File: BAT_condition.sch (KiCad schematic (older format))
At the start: 2 parts

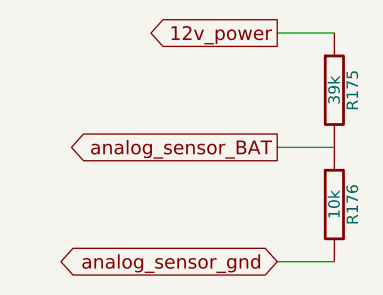
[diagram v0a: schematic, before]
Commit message: Removed LM1815 options. Now adaptive mode and square waves are the default,
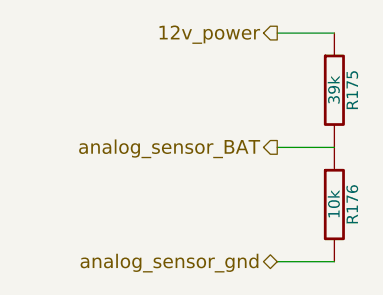
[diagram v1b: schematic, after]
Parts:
- R175: Field1 (none) -> newark,38K0371; Field2 (none) -> vendor1, smd w hem; Field3 (none) -> vendor2, thru w hem; Field4 (none) -> vendor2, smd w hem; Field5 (none) -> 250,mW; Field6 (none) -> 5,%; Field7 (none) -> carbon film; Field8 (none) -> other,more,stuff
- R176: Field1 (none) -> newark,38k0328; Field2 (none) -> vendor1, smd w hem; Field3 (none) -> vendor2, thru w hem; Field4 (none) -> vendor2, smd w hem; Field5 (none) -> 250,mW; Field6 (none) -> 5,%; Field7 (none) -> carbon film; Field8 (none) -> other,more,stuff
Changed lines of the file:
@@
-EESchema Schematic File Version 1
-LIBS:power,./freeEMS_lib,device,conn,linear,regul,74xx,cmos4000,adc-dac,memory,xilinx,special,microcontrollers,dsp,microchip,analog_switches,motorola,texas,intel,audio,interface,digital-audio,philips,display,cypress,siliconi,contrib,valves,./freeEMS_1.cache
+EESchema Schematic File Version 2  date Fri 02 Jul 2010 02:24:35 PM ART
+LIBS:power
+LIBS:freeEMS_lib
+LIBS:device
+LIBS:conn
+LIBS:linear
+LIBS:regul
+LIBS:74xx
+LIBS:cmos4000
+LIBS:adc-dac
+LIBS:memory
+LIBS:xilinx
+LIBS:special
+LIBS:microcontrollers
+LIBS:dsp
+LIBS:microchip
+LIBS:analog_switches
+LIBS:motorola
+LIBS:texas
+LIBS:intel
+LIBS:audio
+LIBS:interface
+LIBS:digital-audio
+LIBS:philips
+LIBS:display
+LIBS:cypress
+LIBS:siliconi
+LIBS:contrib
+LIBS:valves
+LIBS:freeEMS_1-cache
 EELAYER 23  0
 EELAYER END
@@
 Sheet 37 41
 Title "freeEMS 1.0"
-Date "15 nov 2008"
+Date "2 jul 2010"
 Rev "A.20"
 Comp "diyefi.org"
@@
 Wire Wire Line
 	2250 2300 2500 2300
-Text GLabel 2250 1800 0    60   Output
+Text HLabel 2250 1800 0    60   Output ~ 0
 12v_power
 $Comp
@@
 U 1 1 4890FC9B
 P 2500 2550
-F 0 "R176" V 2580 2550 50  0000 C C
-F 1 "10k" V 2500 2550 50  0000 C C
-F 2 "R4-SM0805" V 2680 2650 60  0001 C C
-F 4 "newark,38k0328" V 1130 2600 60  0001 C C
-F 5 "vendor1, smd w hem" V 1130 2600 60  0001 C C
-F 6 "vendor2, thru w hem" V 1130 2600 60  0001 C C
-F 7 "vendor2, smd w hem" V 1130 2600 60  0001 C C
-F 8 "250,mW" V 1130 2600 60  0001 C C
-F 9 "5,%" V 1130 2600 60  0001 C C
-F 10 "carbon film" V 1130 2600 60  0001 C C
-F 11 "other,more,stuff" V 1130 2600 60  0001 C C
+F 0 "R176" V 2580 2550 50  0000 C CNN
+F 1 "10k" V 2500 2550 50  0000 C CNN
+F 2 "R4-SM0805" V 2680 2650 60  0001 C CNN
+F 4 "newark,38k0328" V 1130 2600 60  0001 C CNN "Field1"
+F 5 "vendor1, smd w hem" V 1130 2600 60  0001 C CNN "Field2"
+F 6 "vendor2, thru w hem" V 1130 2600 60  0001 C CNN "Field3"
+F 7 "vendor2, smd w hem" V 1130 2600 60  0001 C CNN "Field4"
+F 8 "250,mW" V 1130 2600 60  0001 C CNN "Field5"
+F 9 "5,%" V 1130 2600 60  0001 C CNN "Field6"
+F 10 "carbon film" V 1130 2600 60  0001 C CNN "Field7"
+F 11 "other,more,stuff" V 1130 2600 60  0001 C CNN "Field8"
 	1    2500 2550
 	1    0    0    -1
@@
 U 1 1 4890FC93
 P 2500 2050
-F 0 "R175" V 2580 2050 50  0000 C C
-F 1 "39k" V 2500 2050 50  0000 C C
-F 2 "R4-SM0805" V 2680 2150 60  0001 C C
-F 4 "newark,38K0371" V 1130 2600 60  0001 C C
-F 5 "vendor1, smd w hem" V 1130 2600 60  0001 C C
-F 6 "vendor2, thru w hem" V 1130 2600 60  0001 C C
-F 7 "vendor2, smd w hem" V 1130 2600 60  0001 C C
-F 8 "250,mW" V 1130 2600 60  0001 C C
-F 9 "5,%" V 1130 2600 60  0001 C C
-F 10 "carbon film" V 1130 2600 60  0001 C C
-F 11 "other,more,stuff" V 1130 2600 60  0001 C C
+F 0 "R175" V 2580 2050 50  0000 C CNN
+F 1 "39k" V 2500 2050 50  0000 C CNN
+F 2 "R4-SM0805" V 2680 2150 60  0001 C CNN
+F 4 "newark,38K0371" V 1130 2600 60  0001 C CNN "Field1"
+F 5 "vendor1, smd w hem" V 1130 2600 60  0001 C CNN "Field2"
+F 6 "vendor2, thru w hem" V 1130 2600 60  0001 C CNN "Field3"
+F 7 "vendor2, smd w hem" V 1130 2600 60  0001 C CNN "Field4"
+F 8 "250,mW" V 1130 2600 60  0001 C CNN "Field5"
+F 9 "5,%" V 1130 2600 60  0001 C CNN "Field6"
+F 10 "carbon film" V 1130 2600 60  0001 C CNN "Field7"
+F 11 "other,more,stuff" V 1130 2600 60  0001 C CNN "Field8"
 	1    2500 2050
 	1    0    0    -1
 $EndComp
-Text GLabel 2250 2800 0    60   BiDi
+Text HLabel 2250 2800 0    60   BiDi ~ 0
 analog_sensor_gnd
-Text GLabel 2250 2300 0    60   Output
+Text HLabel 2250 2300 0    60   Output ~ 0
 analog_sensor_BAT
 $EndSCHEMATC

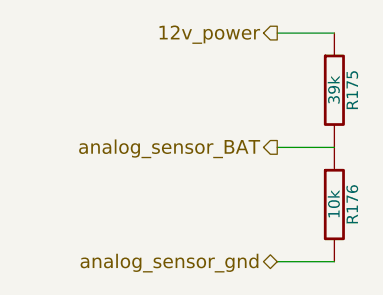
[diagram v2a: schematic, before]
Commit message: Implemented P&H, removed current sense circuitry, removed all unnecessary files from the repo
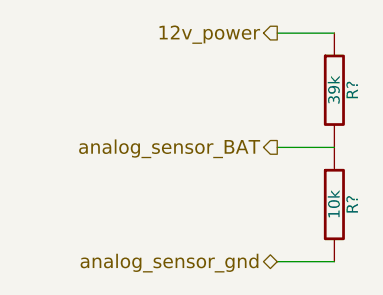
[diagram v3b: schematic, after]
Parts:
- renumbered R175 to R?, R176 to R?
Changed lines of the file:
@@
-EESchema Schematic File Version 2  date Fri 02 Jul 2010 05:44:26 PM ART
+EESchema Schematic File Version 2  date Sat 03 Jul 2010 10:49:02 AM ART
 LIBS:power
 LIBS:freeEMS_lib
@@
 EELAYER END
 $Descr A4 11700 8267
-Sheet 37 41
+Sheet 1 41
 Title "freeEMS 1.0"
-Date "2 jul 2010"
-Rev "A.20"
+Date "3 jul 2010"
+Rev "A.08"
 Comp "diyefi.org"
 Comment1 "BAT_condition"
@@
 12v_power
 $Comp
-L R R176
+L R R?
 U 1 1 4890FC9B
 P 2500 2550
-F 0 "R176" V 2580 2550 50  0000 C CNN
+F 0 "R?" V 2580 2550 50  0000 C CNN
 F 1 "10k" V 2500 2550 50  0000 C CNN
 F 2 "R4-SM0805" V 2680 2650 60  0001 C CNN
@@
 $EndComp
 $Comp
-L R R175
+L R R?
 U 1 1 4890FC93
 P 2500 2050
-F 0 "R175" V 2580 2050 50  0000 C CNN
+F 0 "R?" V 2580 2050 50  0000 C CNN
 F 1 "39k" V 2500 2050 50  0000 C CNN
 F 2 "R4-SM0805" V 2680 2150 60  0001 C CNN

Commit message: Corrected ERC errors by fixing the custom FreeEMS components pinouts
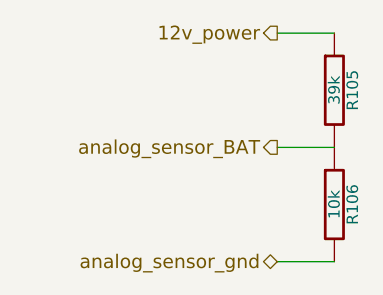
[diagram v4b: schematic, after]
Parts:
- gave numbers to parts that had none: 2
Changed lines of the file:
@@
-EESchema Schematic File Version 2  date Sat 03 Jul 2010 10:49:02 AM ART
+EESchema Schematic File Version 2  date Sat 03 Jul 2010 12:32:24 PM ART
 LIBS:power
 LIBS:freeEMS_lib
@@
 12v_power
 $Comp
-L R R?
+L R R106
 U 1 1 4890FC9B
 P 2500 2550
-F 0 "R?" V 2580 2550 50  0000 C CNN
+F 0 "R106" V 2580 2550 50  0000 C CNN
 F 1 "10k" V 2500 2550 50  0000 C CNN
 F 2 "R4-SM0805" V 2680 2650 60  0001 C CNN
@@
 $EndComp
 $Comp
-L R R?
+L R R105
 U 1 1 4890FC93
 P 2500 2050
-F 0 "R?" V 2580 2050 50  0000 C CNN
+F 0 "R105" V 2580 2050 50  0000 C CNN
 F 1 "39k" V 2500 2050 50  0000 C CNN
 F 2 "R4-SM0805" V 2680 2150 60  0001 C CNN
